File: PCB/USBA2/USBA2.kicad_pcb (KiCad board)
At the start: 2 copper layers, 13.2 x 12.2 mm, 20 parts, among them J1 USB_A, U1 ESP32-PICO-MINI-02, U2 LMR16006YDDCR, U3 CH340X, U4 QR

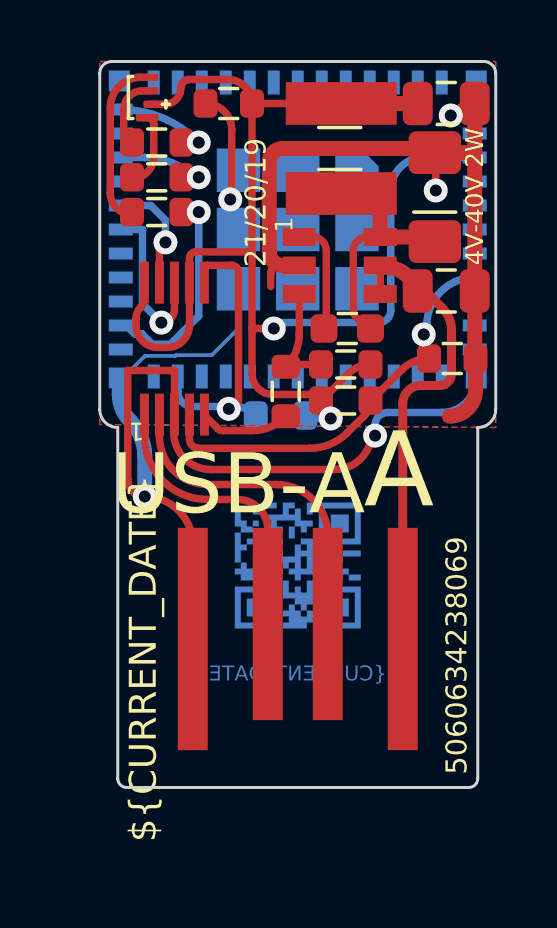
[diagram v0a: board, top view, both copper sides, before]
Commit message: Smaller footprint on CH340X
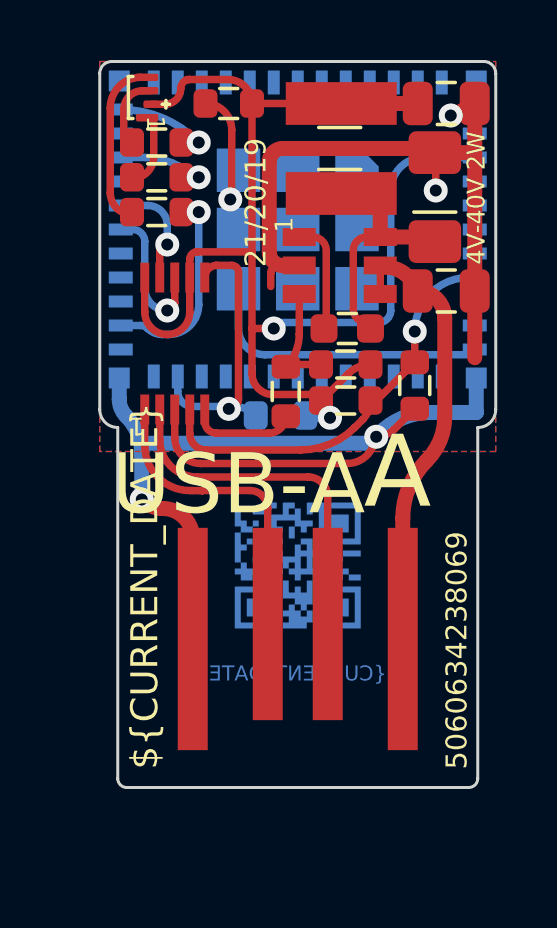
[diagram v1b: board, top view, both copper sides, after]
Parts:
- moved C5 1.54 mm to (125.4, 117.6), turned to 90 degrees
- moved U3 0.17 mm to (117.4, 116.2)
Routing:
- net GND: track 47.1 -> 51.7 mm
- net Net-(J1-D-): track 8.09 -> 11.9 mm
- net DC: track 14.2 -> 13.4 mm
- net I: track 5.65 -> 4.94 mm
- net Net-(J1-D+): track 9.64 -> 10.3 mm
- net +3.3V: track 42.4 -> 41.9 mm

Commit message: Tidy
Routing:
- net +3.3V: track 41.9 -> 40.8 mm
- net GND: track 51.7 -> 52.4 mm, vias 5 -> 4
